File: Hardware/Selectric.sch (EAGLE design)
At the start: 114 parts, among them IC1 MAX3232ESE, Q1 BSP613P, Q10 BSS123, Q11 BSP613P, Q12 BSS123, Q13 BSP613P, Q14 BSS123, Q15 BSP613P, Q16 BSS123, Q17 BSP613P, Q18 BSS123, Q19 BSP613P, Q2 BSS123, Q20 BSS123, Q21 BSP613P, Q22 BSS123, Q23 BSP613P, Q24 BSS123, Q25 BSP613P, Q26 BSS123, Q27 BSP613P, Q28 BSS123, Q29 BSP613P, Q3 BSP613P, Q30 BSS123, Q31 BSP613P, Q32 BSS123, Q4 BSS123, Q5 BSP613P, Q6 BSS123, Q7 BSP613P, Q8 BSS123, Q9 BSP613P

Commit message: Updated schematic and tidied board
Added Arduino 5V power feed. Tidied some traces and labels.
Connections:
- net 5V: now also DC1.+VOUT, IC1P.VCC
- net VCC: no longer DC1.+VOUT, IC1P.VCC
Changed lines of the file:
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@@
-</segment>
-</net>
-<net name="VCC" class="1">
-<segment>
-<label x="210.82" y="144.78" size="1.778" layer="95"/>
-<pinref part="DC1" gate="G$1" pin="+VOUT"/>
-<wire x1="208.28" y1="144.78" x2="215.9" y2="144.78" width="0.1524" layer="91"/>
-<wire x1="215.9" y1="144.78" x2="215.9" y2="147.32" width="0.1524" layer="91"/>
-<pinref part="IC1" gate="P" pin="VCC"/>
-<wire x1="215.9" y1="147.32" x2="223.52" y2="147.32" width="0.1524" layer="91"/>
 </segment>
 </net>
@@
 <pinref part="JP10" gate="G$1" pin="3"/>
 </segment>
+<segment>
+<label x="210.82" y="144.78" size="1.778" layer="95"/>
+<pinref part="DC1" gate="G$1" pin="+VOUT"/>
+<wire x1="208.28" y1="144.78" x2="215.9" y2="144.78" width="0.1524" layer="91"/>
+<wire x1="215.9" y1="144.78" x2="215.9" y2="147.32" width="0.1524" layer="91"/>
+<pinref part="IC1" gate="P" pin="VCC"/>
+<wire x1="215.9" y1="147.32" x2="223.52" y2="147.32" width="0.1524" layer="91"/>
+</segment>
 </net>

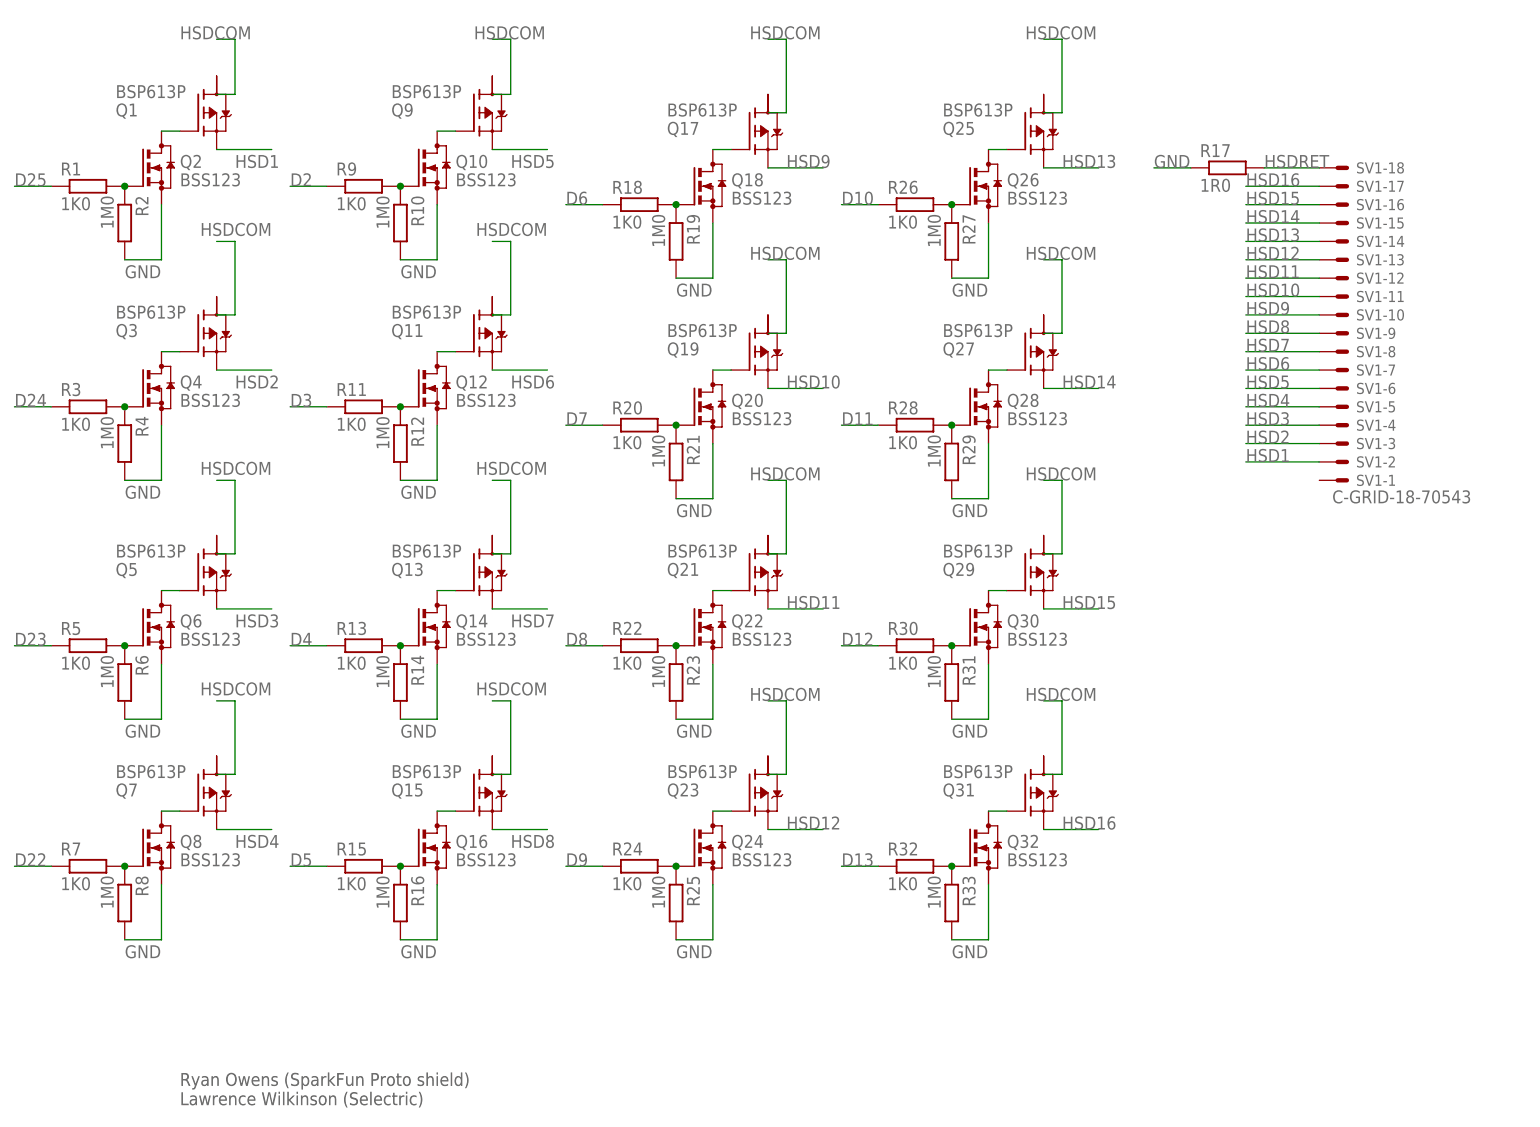
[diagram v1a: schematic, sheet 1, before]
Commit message: Modify to use Allegro A2982SLW-T drivers
Replace discrete mosfets with A2982 driver ICs.
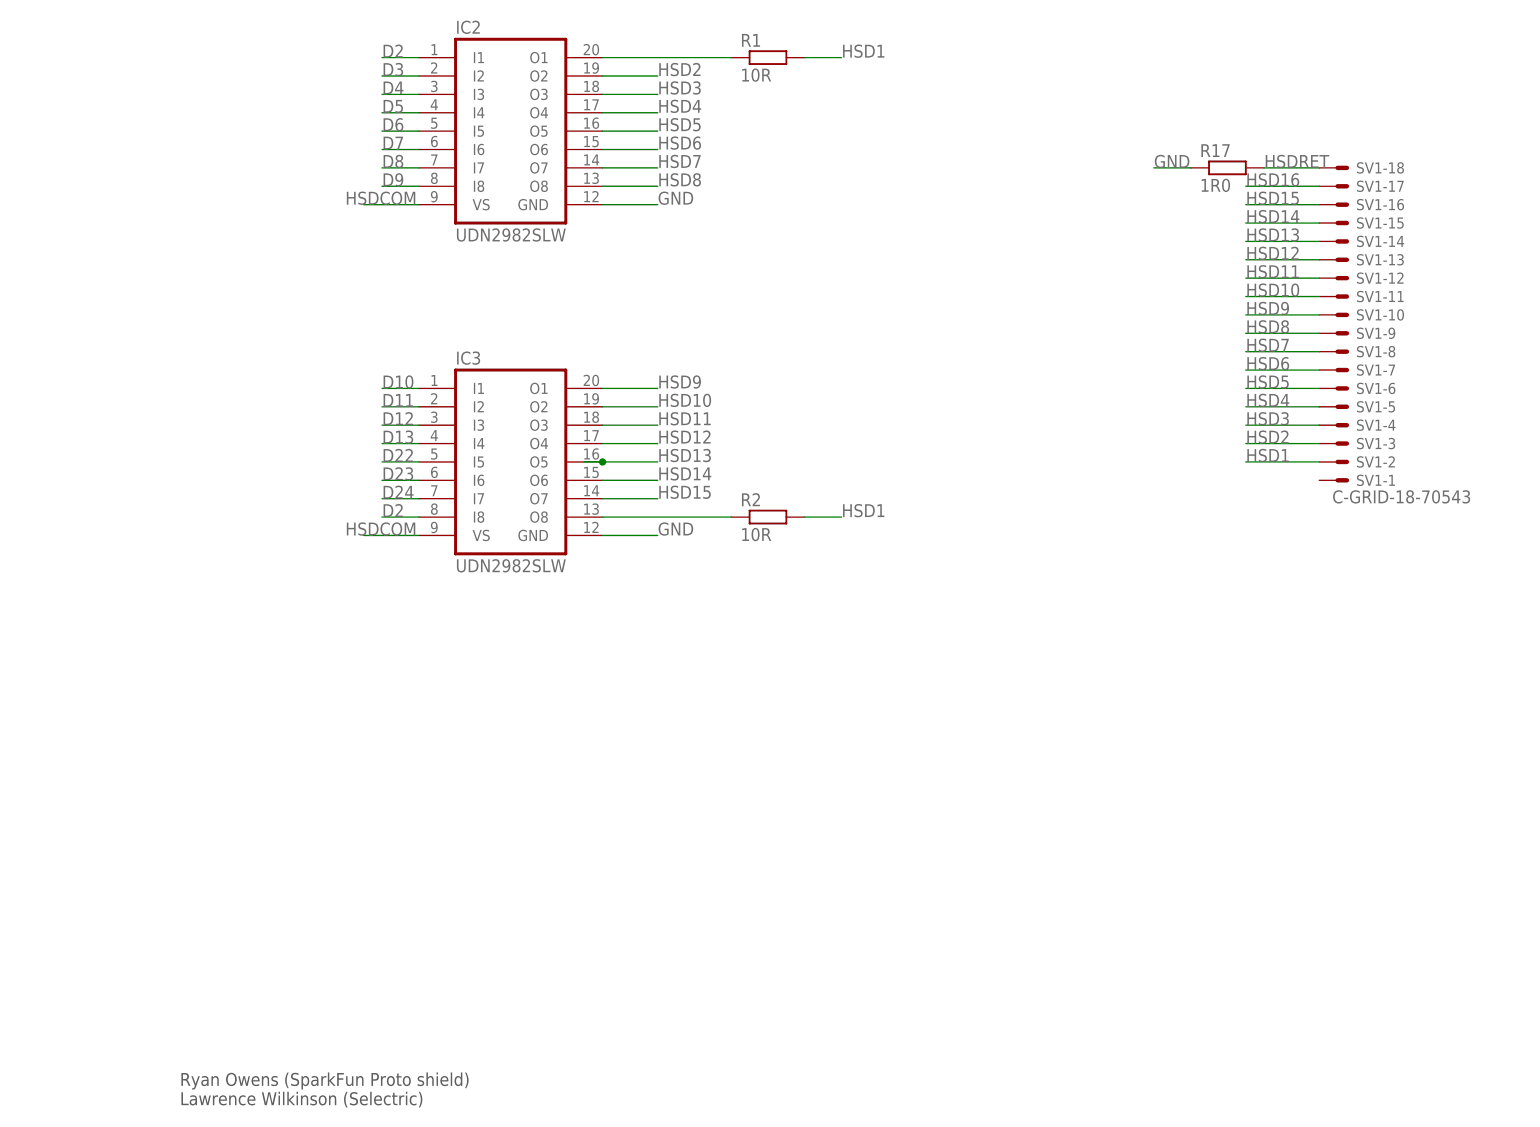
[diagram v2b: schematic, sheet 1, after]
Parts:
- removed Q1, Q11, Q13, Q15, Q17, Q19, Q21, Q23, Q25, Q27, Q29, Q3, Q31, Q5, Q7, Q9: BSP613P, infineon:BSP613P
- removed Q10, Q12, Q14, Q16, Q18, Q2, Q20, Q22, Q24, Q26, Q28, Q30, Q32, Q4, Q6, Q8: BSS123, transistor-small-signal:BSS123
- removed R10, R12, R14, R16, R19, R21, R23, R25, R27, R29, R31, R33, R4, R6, R8: 1M0, rcl:R-EU_R0603
- removed R11, R13, R15, R18, R20, R22, R24, R26, R28, R3, R30, R32, R5, R7, R9: 1K0, rcl:R-EU_R0603
- added IC2, IC3: UDN2982SLW, uln-udn:UDN2982SLW
- R1: value 1K0 -> 10R; device rcl:R-EU_R0603 -> rcl:R-EU_M1206
- R2: value 1M0 -> 10R; device rcl:R-EU_R0603 -> rcl:R-EU_M1206
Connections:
- removed net N$10: Q3.G, Q4.D
- removed net N$11: Q6.G, R5.2, R6.1
- removed net N$12: Q5.G, Q6.D
- removed net N$13: Q8.G, R7.2, R8.1
- removed net N$14: Q7.G, Q8.D
- removed net N$15: Q10.G, R10.1, R9.2
- removed net N$16: Q10.D, Q9.G
- removed net N$17: Q12.G, R11.2, R12.1
- removed net N$18: Q11.G, Q12.D
- removed net N$19: Q14.G, R13.2, R14.1
- removed net N$20: Q13.G, Q14.D
- removed net N$21: Q16.G, R15.2, R16.1
- removed net N$22: Q15.G, Q16.D
- removed net N$26: Q18.G, R18.2, R19.1
- removed net N$27: Q17.G, Q18.D
- removed net N$28: Q20.G, R20.2, R21.1
- removed net N$29: Q19.G, Q20.D
- removed net N$30: Q22.G, R22.2, R23.1
- removed net N$31: Q21.G, Q22.D
- removed net N$32: Q24.G, R24.2, R25.1
- removed net N$33: Q23.G, Q24.D
- removed net N$34: Q26.G, R26.2, R27.1
- removed net N$35: Q25.G, Q26.D
- removed net N$36: Q28.G, R28.2, R29.1
- removed net N$37: Q27.G, Q28.D
- removed net N$38: Q30.G, R30.2, R31.1
- removed net N$39: Q29.G, Q30.D
- removed net N$40: Q32.G, R32.2, R33.1
- removed net N$41: Q31.G, Q32.D
- removed net N$9: Q1.G, Q2.D
- net D10: now also IC3.I1; no longer R26.1
- net D11: now also IC3.I2; no longer R28.1
- net D12: now also IC3.I3; no longer R30.1
- net D13: now also IC3.I4; no longer R32.1
- net D2: now also IC2.I1, IC3.I8; no longer R9.1
- net D22: now also IC3.I5; no longer R7.1
- net D23: now also IC3.I6; no longer R5.1
- net D24: now also IC3.I7; no longer R3.1
- net D25: no longer R1.1
- net D3: now also IC2.I2; no longer R11.1
- net D4: now also IC2.I3; no longer R13.1
- net D5: now also IC2.I4; no longer R15.1
- net D6: now also IC2.I5; no longer R18.1
- net D7: now also IC2.I6; no longer R20.1
- net D8: now also IC2.I7; no longer R22.1
- net D9: now also IC2.I8; no longer R24.1
- net GND: now also IC2.GND, IC3.GND; no longer Q10.S, Q12.S, Q14.S, Q16.S, Q18.S, Q2.S, Q20.S, Q22.S, Q24.S, Q26.S, Q28.S, Q30.S, Q32.S, Q4.S, Q6.S, Q8.S, R10.2, R12.2, R14.2, R16.2, R19.2, R2.2, R21.2, R23.2, R25.2, R27.2, R29.2, R31.2, R33.2, R4.2, R6.2, R8.2
- net HSD1: now also R1.2, R2.2; no longer Q1.S
- net HSD10: now also IC3.O2; no longer Q19.S
- net HSD11: now also IC3.O3; no longer Q21.S
- net HSD12: now also IC3.O4; no longer Q23.S
- net HSD13: now also IC3.O5; no longer Q25.S
- net HSD14: now also IC3.O6; no longer Q27.S
- net HSD15: now also IC3.O7; no longer Q29.S
- net HSD16: no longer Q31.S
- net HSD2: now also IC2.O2; no longer Q3.S
- net HSD3: now also IC2.O3; no longer Q5.S
- net HSD4: now also IC2.O4; no longer Q7.S
- net HSD5: now also IC2.O5; no longer Q9.S
- net HSD6: now also IC2.O6; no longer Q11.S
- net HSD7: now also IC2.O7; no longer Q13.S
- net HSD8: now also IC2.O8; no longer Q15.S
- net HSD9: now also IC3.O1; no longer Q17.S
- net HSDCOM: now also IC2.VS, IC3.VS; no longer Q1.D@2, Q11.D@2, Q13.D@2, Q15.D@2, Q17.D@2, Q19.D@2, Q21.D@2, Q23.D@2, Q25.D@2, Q27.D@2, Q29.D@2, Q3.D@2, Q31.D@2, Q5.D@2, Q7.D@2, Q9.D@2
- net N$5: now also IC3.O8; no longer Q2.G, R1.2
- net N$8: now also IC2.O1, R1.1; no longer Q4.G, R3.2, R4.1
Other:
- moved on the sheet: R1, R2

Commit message: Add switch/LED header J2
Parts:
- added J2: 22-23-2041, con-molex:22-23-2041
- added R3, R4: 220R, rcl:R-EU_M1206
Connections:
- removed net 5V: DC1.+VOUT, IC1P.VCC, JP10.3
- new net LED+: J2-4.S, R4.2
- net D52: now also J2-2.S, R3.2
- net D53: now also R4.1
- net GND: now also J2-1.S, J2-3.S
- net VCC: now also DC1.+VOUT, IC1P.VCC, JP10.3, R3.1
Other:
- note added: "Analogue Inputs A0 HSDRET A1 HSDGND"
- note added: "Keyboard Inputs D38 D39 D40 D41 D42 D43 D44 D45 D46 D47 D48 D49 D50 D51"
- note added: "Other Inputs D0 RXD D17 CTS D52 Switch"
- note added: "Other Outputs D1 TXD D16 RTS D53 LED"
- note added: "Printer Switch Inputs D26 D27 D28 D29 D30 D31 D32 D33 D34 D35 D36 D37"
- note added: "Solenoid Outputs D2 LOCK D3 D4 D5 D6 D7 D8 D9 D10 D11 D12 D22 D23 D24"
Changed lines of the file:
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@@
 <part name="R2" library="rcl" deviceset="R-EU_" device="M1206" value="10R"/>
 <part name="R1" library="rcl" deviceset="R-EU_" device="M1206" value="10R"/>
+<part name="J2" library="con-molex" deviceset="22-23-2041" device=""/>
+<part name="R3" library="rcl" deviceset="R-EU_" device="M1206" value="220R"/>
+<part name="R4" library="rcl" deviceset="R-EU_" device="M1206" value="220R"/>
 </parts>
 <sheets>
@@
 <sheet>
 <plain>
+<text x="147.32" y="137.16" size="1.778" layer="91">Solenoid Outputs
+D2 LOCK
+D3
+D4
+D5
+D6
+D7
+D8
+D9
+D10
+D11
+D12
+D22
+D23
+D24</text>
+<text x="185.42" y="167.64" size="1.778" layer="91">Other Outputs
+D1 TXD
+D16 RTS
+D53 LED</text>
+<text x="147.32" y="78.74" size="1.778" layer="91">Printer Switch Inputs
+D26
+D27
+D28
+D29
+D30
+D31
+D32
+D33
+D34
+D35
+D36
+D37</text>
+<text x="210.82" y="66.04" size="1.778" layer="91">Keyboard Inputs
+D38
+D39
+D40
+D41
+D42
+D43
+D44
+D45
+D46
+D47
+D48
+D49
+D50
+D51</text>
+<text x="147.32" y="66.04" size="1.778" layer="91">Other Inputs
+D0 RXD
+D17 CTS
+D52 Switch</text>
+<text x="147.32" y="50.8" size="1.778" layer="91">Analogue Inputs
+A0 HSDRET
+A1 HSDGND</text>
 </plain>
 <instances>
@@
 <instance part="JP8" gate="G$1" x="55.88" y="81.28"/>
 <instance part="JP9" gate="G$1" x="55.88" y="78.74" rot="R180"/>
+<instance part="J2" gate="-1" x="60.96" y="35.56"/>
+<instance part="J2" gate="-2" x="60.96" y="30.48"/>
+<instance part="J2" gate="-3" x="60.96" y="25.4"/>
+<instance part="J2" gate="-4" x="60.96" y="20.32"/>
+<instance part="R3" gate="G$1" x="27.94" y="30.48"/>
+<instance part="R4" gate="G$1" x="27.94" y="20.32"/>
 </instances>
 <busses>
@@
 <junction x="93.98" y="129.54"/>
 </segment>
+<segment>
+<pinref part="R3" gate="G$1" pin="1"/>
+<wire x1="10.16" y1="30.48" x2="22.86" y2="30.48" width="0.1524" layer="91"/>
+<label x="10.16" y="30.48" size="1.778" layer="95"/>
+</segment>
 </net>
 <net name="D22" class="0">
@@
 <net name="D52" class="0">
 <segment>
-<wire x1="43.18" y1="60.96" x2="45.72" y2="60.96" width="0.1524" layer="91"/>
-<label x="42.672" y="62.484" size="1.778" layer="95" rot="R180"/>
+<label x="37.592" y="59.944" size="1.778" layer="95" rot="R180"/>
 <pinref part="JP9" gate="G$1" pin="16"/>
+<pinref part="R3" gate="G$1" pin="2"/>
+<pinref part="J2" gate="-2" pin="S"/>
+<wire x1="33.02" y1="30.48" x2="38.1" y2="30.48" width="0.1524" layer="91"/>
+<label x="45.72" y="30.48" size="1.778" layer="95"/>
+<wire x1="38.1" y1="30.48" x2="58.42" y2="30.48" width="0.1524" layer="91"/>
+<wire x1="45.72" y1="60.96" x2="38.1" y2="60.96" width="0.1524" layer="91"/>
+<wire x1="38.1" y1="60.96" x2="38.1" y2="30.48" width="0.1524" layer="91"/>
+<junction x="38.1" y="30.48"/>
 </segment>
 </net>
@@
 <pinref part="JP8" gate="G$1" pin="1"/>
 </segment>
+<segment>
+<pinref part="R4" gate="G$1" pin="1"/>
+<wire x1="10.16" y1="20.32" x2="22.86" y2="20.32" width="0.1524" layer="91"/>
+<label x="10.16" y="20.32" size="1.778" layer="95"/>
+</segment>
 </net>
 <net name="D23" class="0">
@@
 <label x="74.168" y="99.822" size="1.778" layer="95" rot="R180"/>
 <pinref part="JP8" gate="G$1" pin="16"/>
+</segment>
+</net>
+<net name="GND" class="1">
+<segment>
+<pinref part="J2" gate="-1" pin="S"/>
+<wire x1="45.72" y1="35.56" x2="58.42" y2="35.56" width="0.1524" layer="91"/>
+<label x="45.72" y="35.56" size="1.778" layer="95"/>
+<junction x="58.42" y="35.56"/>
+</segment>
+<segment>
+<wire x1="45.72" y1="25.4" x2="58.42" y2="25.4" width="0.1524" layer="91"/>
+<label x="45.72" y="25.4" size="1.778" layer="95"/>
+<pinref part="J2" gate="-3" pin="S"/>
+<junction x="58.42" y="25.4"/>
+</segment>
+</net>
+<net name="LED+" class="0">
+<segment>
+<pinref part="R4" gate="G$1" pin="2"/>
+<pinref part="J2" gate="-4" pin="S"/>
+<wire x1="33.02" y1="20.32" x2="58.42" y2="20.32" width="0.1524" layer="91"/>
+<label x="45.72" y="20.32" size="1.778" layer="95"/>
 </segment>
 </net>
@@
 </segment>
 </net>
-<net name="5V" class="0">
+<net name="VCC" class="1">
 <segment>
 <wire x1="99.06" y1="71.12" x2="96.52" y2="71.12" width="0.1524" layer="91"/>

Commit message: Finalise components and values. add BoM
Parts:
- removed JP12: (no value), SparkFun:M02LOCK
- removed R36, R54: 220R, rcl:R-EU_M1206
- removed SV2: (no value), con-lstb:MA13-2
- added JP2: M16LOCK, SparkFun:M16LOCK
- added R10: 1K, rcl:R-EU_M1206
- added R11: 220R, rcl:R-EU_M1206
- added X3: (no value), con-subd:F09HP
- DC1: value TMR -> TMR1-4811; device traco_tmr:TMR -> traco_tmr:TMR1-4811
- IC1: value MAX3232ESE -> UDN2982SLW; device maxim:MAX3232ESE -> uln-udn:UDN2982SLW
- IC3: value UDN2982SLW -> MAX3232ESE; device uln-udn:UDN2982SLW -> maxim:MAX3232ESE
- JP1: value (none) -> M16LOCK; device pinhead:PINHD-2X2 -> SparkFun:M16LOCK
- JP10: device SparkFun:M06LOCK -> SparkFun:M08LOCK
- JP11: device SparkFun:M02LOCK -> SparkFun:M08LOCK
- JP3, JP4: device SparkFun:M08LOCK -> SparkFun:M02LOCK
- JP5: device SparkFun:M08LOCK -> SparkFun:M06LOCK
- JP7: device SparkFun:M08LOCK -> pinhead:PINHD-2X2
- JP8, JP9: value M16LOCK -> (none); device SparkFun:M16LOCK -> SparkFun:M08LOCK
- R12, R13, R14, R15, R16, R18, R19, R20, R21, R22, R23, R24, R25, R26, R27, R28, R29, R30, R31, R4, R5, R6, R7, R8, R9: value 220R -> 1K
- R17: value 1R0 -> 1K; device rcl:R-EU_0922/22 -> rcl:R-EU_M1206
- R3: value 220R -> 1R0; device rcl:R-EU_M1206 -> rcl:R-EU_0922/22
- SV1: value C-GRID-18-70543 -> (none); device con-molex:C-GRID-18-70543 -> con-lstb:MA13-2
- X1: value (none) -> C-GRID-18-70543; device con-subd:F09HP -> con-molex:C-GRID-18-70543
- renumbered J2 to X2, R34 to R12, R35 to R19, R37 to R26, R38 to R13, R39 to R20, R40 to R5, R41 to R27, R42 to R14, R43 to R21, R44 to R6, R45 to R28, R46 to R15, R47 to R22, R48 to R7, R49 to R29, R50 to R16, R51 to R23, R52 to R8, R53 to R30, R55 to R24, R56 to R9, R57 to R31, R58 to R18, R59 to R25
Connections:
- net 3.3: now also JP5.2; no longer JP10.2
- net 5V@1: now also JP3.1, JP3.2; no longer JP12.1, JP12.2
- net A10: now also JP10.3; no longer JP6.3
- net A11: now also JP10.4; no longer JP6.4
- net A12: now also JP10.5; no longer JP6.5
- net A13: now also JP10.6; no longer JP6.6
- net A14: now also JP10.7; no longer JP6.7
- net A15: now also JP10.8; no longer JP6.8
- net A2: now also JP8.3; no longer JP7.3
- net A3: now also JP8.4; no longer JP7.4
- net A4: now also JP8.5; no longer JP7.5
- net A5: now also JP8.6; no longer JP7.6
- net A6: now also JP8.7; no longer JP7.7
- net A7: now also JP8.8; no longer JP7.8
- net A8: now also JP10.1; no longer JP6.1
- net A9: now also JP10.2; no longer JP6.2
- net AREF: now also JP6.8; no longer JP3.8
- net CTS: now also IC3G$1.R2IN, X3.8; no longer IC1G$1.R2IN, X1.8
- net D10: now also IC2.I1, JP6.3; no longer IC3.I1, JP3.3
- net D11: now also IC2.I2, JP6.4; no longer IC3.I2, JP3.4
- net D12: now also IC2.I3, JP6.5; no longer IC3.I3, JP3.5
- net D13: now also IC2.I4, JP6.6; no longer IC3.I4, JP3.6
- net D14: now also JP11.8; no longer JP5.8
- net D15: now also JP11.7; no longer JP5.7
- net D2: now also IC1.I1, IC2.I8, JP9.3; no longer IC2.I1, IC3.I8, JP4.3
- net D22: now also IC2.I5, JP2.1; no longer IC3.I5, JP9.1
- net D23: now also IC2.I6, JP1.16; no longer IC3.I6, JP8.16
- net D24: now also IC2.I7, JP2.2; no longer IC3.I7, JP9.2
- net D25: now also JP1.15; no longer JP8.15
- net D26: now also JP2.3, SV1.2; no longer JP9.3, SV2.2
- net D27: now also JP1.14, SV1.1; no longer JP8.14, SV2.1
- net D28: now also JP2.4, SV1.4; no longer JP9.4, SV2.4
- net D29: now also JP1.13, R4.2, SV1.3; no longer JP8.13, R36.2, SV2.3
- net D3: now also IC1.I2, JP9.4; no longer IC2.I2, JP4.4
- net D30: now also JP2.5, SV1.6; no longer JP9.5, SV2.6
- net D31: now also JP1.12, SV1.5; no longer JP8.12, SV2.5
- net D32: now also JP2.6, SV1.8; no longer JP9.6, SV2.8
- net D33: now also JP1.11, SV1.7; no longer JP8.11, SV2.7
- net D34: now also JP2.7, SV1.10; no longer JP9.7, SV2.10
- net D35: now also JP1.10, SV1.9; no longer JP8.10, SV2.9
- net D36: now also JP2.8, SV1.12; no longer JP9.8, SV2.12
- net D37: now also JP1.9, SV1.11; no longer JP8.9, SV2.11
- net D38: now also JP2.9, SV1.14; no longer JP9.9, SV2.14
- net D39: now also JP1.8, SV1.13; no longer JP8.8, SV2.13
- net D4: now also IC1.I3, JP9.5; no longer IC2.I3, JP4.5
- net D40: now also JP2.10, SV1.16; no longer JP9.10, SV2.16
- net D41: now also JP1.7, SV1.15; no longer JP8.7, SV2.15
- net D42: now also JP2.11, SV1.18; no longer JP9.11, SV2.18
- net D43: now also JP1.6, SV1.17; no longer JP8.6, SV2.17
- net D44: now also JP2.12, SV1.20; no longer JP9.12, SV2.20
- net D45: now also JP1.5, SV1.19; no longer JP8.5, SV2.19
- net D46: now also JP2.13, SV1.22; no longer JP9.13, SV2.22
- net D47: now also JP1.4, R17.2, SV1.21; no longer JP8.4, R54.2, SV2.21
- net D48: now also JP2.14, SV1.24; no longer JP9.14, SV2.24
- net D49: now also JP1.3, SV1.23; no longer JP8.3, SV2.23
- net D5: now also IC1.I4, JP9.6; no longer IC2.I4, JP4.6
- net D50: now also JP2.15, SV1.26; no longer JP9.15, SV2.26
- net D51: now also JP1.2, SV1.25; no longer JP8.2, SV2.25
- net D52: now also JP2.16, R10.2; no longer JP9.16, R3.2
- net D53: now also JP1.1, R11.1; no longer JP8.1, R4.1
- net D6: now also IC1.I5, JP9.7; no longer IC2.I5, JP4.7
- net D7: now also IC1.I6, JP9.8; no longer IC2.I6, JP4.8
- net D8: now also IC1.I7, JP6.1; no longer IC2.I7, JP3.1
- net D9: now also IC1.I8, JP6.2; no longer IC2.I8, JP3.2
- net GND: now also IC1.GND, IC3P.GND, JP5.4, JP5.5, JP6.7, JP8.2, R3.1, X3.5; no longer IC1P.GND, IC3.GND, JP1.2, JP10.4, JP10.5, JP3.7, R17.1, X1.5
- net HSD1: now also X1-2.S; no longer SV1-2.S
- net HSD10: now also IC2.O2, X1-11.S; no longer IC3.O2, SV1-11.S
- net HSD11: now also IC2.O3, X1-12.S; no longer IC3.O3, SV1-12.S
- net HSD12: now also IC2.O4, X1-13.S; no longer IC3.O4, SV1-13.S
- net HSD13: now also IC2.O5, X1-14.S; no longer IC3.O5, SV1-14.S
- net HSD14: now also IC2.O6, X1-15.S; no longer IC3.O6, SV1-15.S
- net HSD15: now also IC2.O7, X1-16.S; no longer IC3.O7, SV1-16.S
- net HSD16: now also X1-17.S; no longer SV1-17.S
- net HSD2: now also IC1.O2, X1-3.S; no longer IC2.O2, SV1-3.S
- net HSD3: now also IC1.O3, X1-4.S; no longer IC2.O3, SV1-4.S
- net HSD4: now also IC1.O4, X1-5.S; no longer IC2.O4, SV1-5.S
- net HSD5: now also IC1.O5, X1-6.S; no longer IC2.O5, SV1-6.S
- net HSD6: now also IC1.O6, X1-7.S; no longer IC2.O6, SV1-7.S
- net HSD7: now also IC1.O7, X1-8.S; no longer IC2.O7, SV1-8.S
- net HSD8: now also IC1.O8, X1-9.S; no longer IC2.O8, SV1-9.S
- net HSD9: now also IC2.O1, X1-10.S; no longer IC3.O1, SV1-10.S
- net HSDCOM: now also IC1.VS; no longer IC3.VS
- net HSDRET: now also JP8.1, R3.2, X1-18.S; no longer JP7.1, R17.2, SV1-18.S
- net IN_GND: now also JP4.1, JP4.2; no longer JP11.1, JP11.2
- net LED+: now also R11.2; no longer R4.2
- net N$1: now also IC3G$1.C1+; no longer IC1G$1.C1+
- net N$2: now also IC3G$1.C2+; no longer IC1G$1.C2+
- net N$23: now also JP7.4; no longer JP1.4
- net N$24: now also JP7.1; no longer JP1.1
- net N$3: now also IC3G$1.C1-; no longer IC1G$1.C1-
- net N$4: now also IC3G$1.C2-; no longer IC1G$1.C2-
- net N$42: now also JP7.3; no longer JP1.3
- net N$5: now also IC2.O8; no longer IC3.O8
- net N$6: now also C4.1, IC3G$1.V+; no longer C3.1, IC1G$1.V+
- net N$7: now also C3.1, IC3G$1.V-; no longer C4.1, IC1G$1.V-
- net N$8: now also IC1.O1; no longer IC2.O1
- net RES: now also JP5.1; no longer JP10.1
- net RTS: now also IC3G$1.T2OUT, X3.7; no longer IC1G$1.T2OUT, X1.7
- net RX0: now also JP9.1; no longer JP4.1
- net RX1: now also IC3G$1.R1OUT, JP11.3; no longer IC1G$1.R1OUT, JP5.3
- net RX2: now also IC3G$1.R2OUT, JP11.5; no longer IC1G$1.R2OUT, JP5.5
- net RXD: now also IC3G$1.R1IN, X3.2; no longer IC1G$1.R1IN, X1.2
- net SCL: now also JP11.1; no longer JP5.1
- net SDA: now also JP11.2; no longer JP5.2
- net TX0: now also JP9.2; no longer JP4.2
- net TX1: now also IC3G$1.T1IN, JP11.4; no longer IC1G$1.T1IN, JP5.4
- net TX2: now also IC3G$1.T2IN, JP11.6; no longer IC1G$1.T2IN, JP5.6
- net TXD: now also IC3G$1.T1OUT, X3.3; no longer IC1G$1.T1OUT, X1.3
- net VCC: now also IC3P.VCC, JP5.3, R10.1, R17.1, R4.1; no longer IC1P.VCC, JP10.3, R3.1, R36.1, R54.1
- net VIN: now also JP5.6; no longer JP10.6
